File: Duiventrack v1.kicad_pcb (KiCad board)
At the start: 2 copper layers, 22.6 x 12.8 mm, 28 parts, among them P1 CONN_01X07, P2 CONN_01X02, U1 MCP1711-SOT23-5, U2 SP-ABZ-G

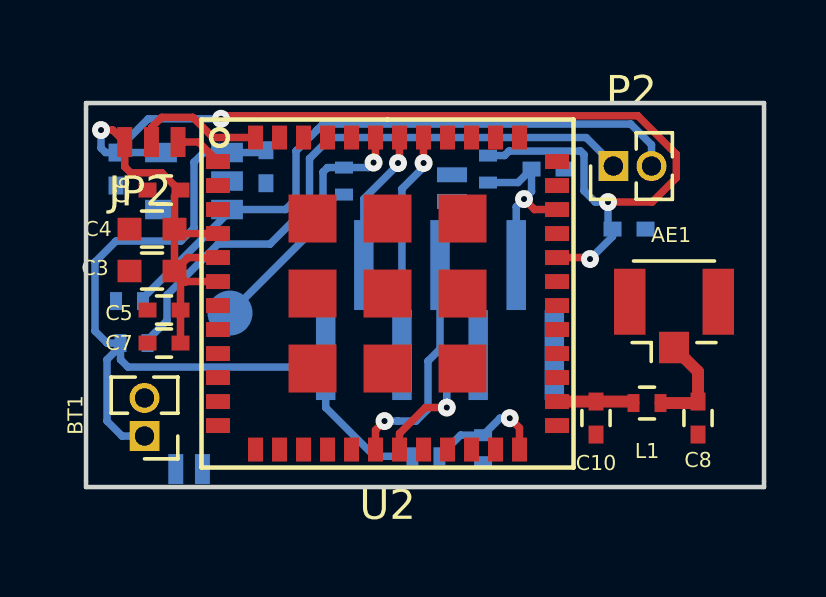
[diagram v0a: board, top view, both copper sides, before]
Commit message: Add via's
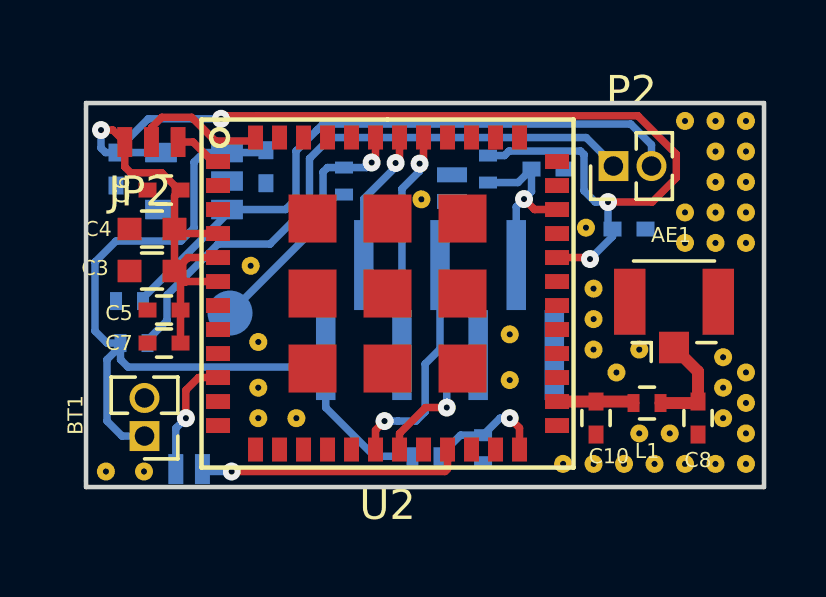
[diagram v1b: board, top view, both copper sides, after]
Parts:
- added REF**: Via 0,6 0,2, Footprint:Via0,6, F.Cu at (151.0, 88.2)
- added REF**: Via 0,6 0,2, Footprint:Via0,6, F.Cu at (159.3, 96.0)
- added REF**: Via 0,6 0,2, Footprint:Via0,6, F.Cu at (156.7, 97.0)
- added REF**: Via 0,6 0,2, Footprint:Via0,6, F.Cu at (157.7, 97.0)
- added REF**: Via 0,6 0,2, Footprint:Via0,6, F.Cu at (158.8, 97.0)
- added REF**: Via 0,6 0,2, Footprint:Via0,6, F.Cu at (159.8, 97.0)
- added REF**: Via 0,6 0,2, Footprint:Via0,6, F.Cu at (160.8, 97.0)
- added REF**: Via 0,6 0,2, Footprint:Via0,6, F.Cu at (161.8, 97.0)
- added REF**: Via 0,6 0,2, Footprint:Via0,6, F.Cu at (161.8, 96.0)
- added REF**: Via 0,6 0,2, Footprint:Via0,6, F.Cu at (161.8, 95.0)
- added REF**: Via 0,6 0,2, Footprint:Via0,6, F.Cu at (161.8, 94.0)
- added REF**: Via 0,6 0,2, Footprint:Via0,6, F.Cu at (161.0, 95.5)
- added REF**: Via 0,6 0,2, Footprint:Via0,6, F.Cu at (160.8, 86.6)
- added REF**: Via 0,6 0,2, Footprint:Via0,6, F.Cu at (160.8, 87.6)
- added REF**: Via 0,6 0,2, Footprint:Via0,6, F.Cu at (160.8, 88.6)
- added REF**: Via 0,6 0,2, Footprint:Via0,6, F.Cu at (159.8, 88.6)
- added REF**: Via 0,6 0,2, Footprint:Via0,6, F.Cu at (159.8, 89.7)
- added REF**: Via 0,6 0,2, Footprint:Via0,6, F.Cu at (160.8, 89.7)
- added REF**: Via 0,6 0,2, Footprint:Via0,6, F.Cu at (161.8, 89.7)
- added REF**: Via 0,6 0,2, Footprint:Via0,6, F.Cu at (161.8, 88.6)
- added REF**: Via 0,6 0,2, Footprint:Via0,6, F.Cu at (161.8, 87.6)
- added REF**: Via 0,6 0,2, Footprint:Via0,6, F.Cu at (161.8, 86.6)
- added REF**: Via 0,6 0,2, Footprint:Via0,6, F.Cu at (161.0, 94.5)
- added REF**: Via 0,6 0,2, Footprint:Via0,6, F.Cu at (161.8, 85.6)
- added REF**: Via 0,6 0,2, Footprint:Via0,6, F.Cu at (160.8, 85.6)
- added REF**: Via 0,6 0,2, Footprint:Via0,6, F.Cu at (159.8, 85.6)
- added REF**: Via 0,6 0,2, Footprint:Via0,6, F.Cu at (158.2, 93.2)
- added REF**: Via 0,6 0,2, Footprint:Via0,6, F.Cu at (156.7, 93.2)
- added REF**: Via 0,6 0,2, Footprint:Via0,6, F.Cu at (156.7, 92.2)
- added REF**: Via 0,6 0,2, Footprint:Via0,6, F.Cu at (156.7, 91.2)
- added REF**: Via 0,6 0,2, Footprint:Via0,6, F.Cu at (155.7, 97.0)
- added REF**: Via 0,6 0,2, Footprint:Via0,6, F.Cu at (153.9, 92.7)
- added REF**: Via 0,6 0,2, Footprint:Via0,6, F.Cu at (153.9, 94.2)
- added REF**: Via 0,6 0,2, Footprint:Via0,6, F.Cu at (161.0, 93.5)
- added REF**: Via 0,6 0,2, Footprint:Via0,6, F.Cu at (146.8, 95.5)
- added REF**: Via 0,6 0,2, Footprint:Via0,6, F.Cu at (145.5, 93.0)
- added REF**: Via 0,6 0,2, Footprint:Via0,6, F.Cu at (145.5, 95.5)
- added REF**: Via 0,6 0,2, Footprint:Via0,6, F.Cu at (145.5, 94.5)
- added REF**: Via 0,6 0,2, Footprint:Via0,6, F.Cu at (140.5, 97.3)
- added REF**: Via 0,6 0,2, Footprint:Via0,6, F.Cu at (141.7, 97.3)
- added REF**: Via 0,6 0,2, Footprint:Via0,6, F.Cu at (145.3, 90.4)
- added REF**: Via 0,6 0,2, Footprint:Via0,6, F.Cu at (156.5, 89.2)
- added REF**: Via 0,6 0,2, Footprint:Via0,6, F.Cu at (157.5, 94.0)
- added REF**: Via 0,6 0,2, Footprint:Via0,6, F.Cu at (158.2, 96.0)
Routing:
- net Net-(JP3-Pad2): track 0.00 -> 8.89 mm, vias 0 -> 1
- net Net-(JP3-Pad1): track 0.00 -> 4.01 mm, vias 0 -> 1

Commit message: All connected and more vias
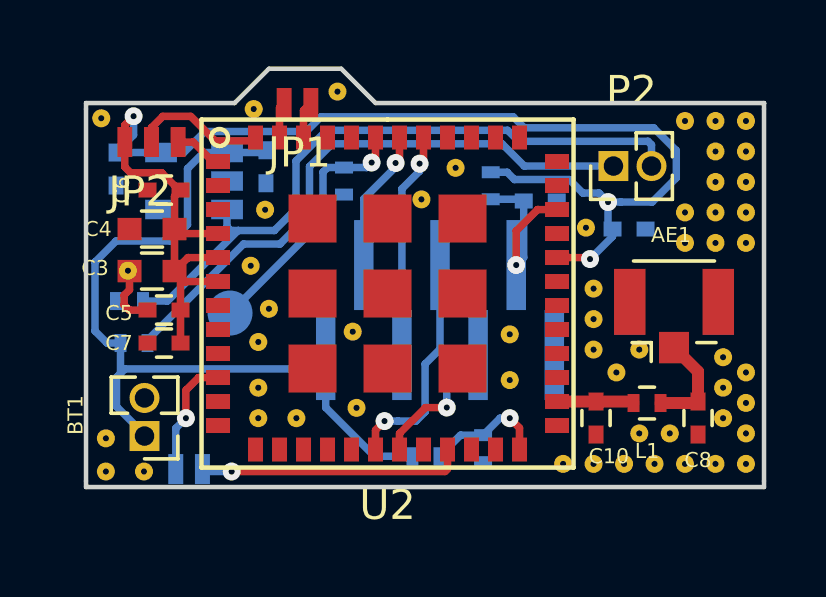
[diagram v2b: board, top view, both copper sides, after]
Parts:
- added REF**: Via 0,6 0,2, Footprint:Via0,6, F.Cu at (145.9, 91.9)
- added REF**: Via 0,6 0,2, Footprint:Via0,6, F.Cu at (148.2, 84.6)
- added REF**: Via 0,6 0,2, Footprint:Via0,6, F.Cu at (140.5, 96.2)
- added REF**: Via 0,6 0,2, Footprint:Via0,6, F.Cu at (152.1, 87.2)
- added REF**: Via 0,6 0,2, Footprint:Via0,6, F.Cu at (148.7, 92.6)
- added REF**: Via 0,6 0,2, Footprint:Via0,6, F.Cu at (148.8, 95.2)
- added REF**: Via 0,6 0,2, Footprint:Via0,6, F.Cu at (145.8, 88.6)
- added REF**: Via 0,6 0,2, Footprint:Via0,6, F.Cu at (141.2, 90.6)
- added REF**: Via 0,6 0,2, Footprint:Via0,6, F.Cu at (140.3, 85.5)
- added REF**: Via 0,6 0,2, Footprint:Via0,6, F.Cu at (145.4, 85.2)
- JP1: moved to F.Cu
- moved JP1 5.86 mm to (146.9, 85.0), turned to 0 degrees
- moved C2 1.10 mm to (154.9, 88.3)
- moved R4 0.56 mm to (153.3, 87.8)
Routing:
- net +3V3: track 49.4 -> 47.1 mm, vias 4 -> 3
- net Earth: track 0.00 -> 2.06 mm
- net VBat: track 29.4 -> 28.0 mm
- net Net-(JP1-Pad2): track 0.00 -> 1.25 mm
- net Net-(JP1-Pad1): track 0.00 -> 1.21 mm
- net Net-(P2-Pad2): track 21.5 -> 22.2 mm
- net Net-(P2-Pad1): track 20.2 -> 19.6 mm
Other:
- board size 22.6 x 12.8 mm -> 22.6 x 13.9 mm

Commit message: Decrease line clearance
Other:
- net class Default: clearance 0.2 -> 0.15
- rule trace_clearance: 0.2 -> 0.15
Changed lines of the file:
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@@
     (links 128)
     (no_connects 0)
-    (area 139.724999 83.781999 162.481001 97.875001)
+    (area 129.550001 80.1 166.259905 100.008)
     (thickness 1.6)
     (drawings 14)
@@
     (user_trace_width 0.45)
     (user_trace_width 0.5)
-    (trace_clearance 0.2)
+    (trace_clearance 0.15)
     (zone_clearance 0.1)
     (zone_45_only no)
@@
   (net 20 "Net-(JP2-Pad3)")
   (net_class Default "This is the default net class."
-    (clearance 0.2)
+    (clearance 0.15)
     (trace_width 0.25)
     (via_dia 0.6)
